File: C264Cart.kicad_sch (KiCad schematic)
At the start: 11 parts, among them J1 SJ, J2 SJ, J3 SJ, J4 SJ, J5 SJ, J6 SJ, U1 23128, U2 23128, U3 264-Exp-Port

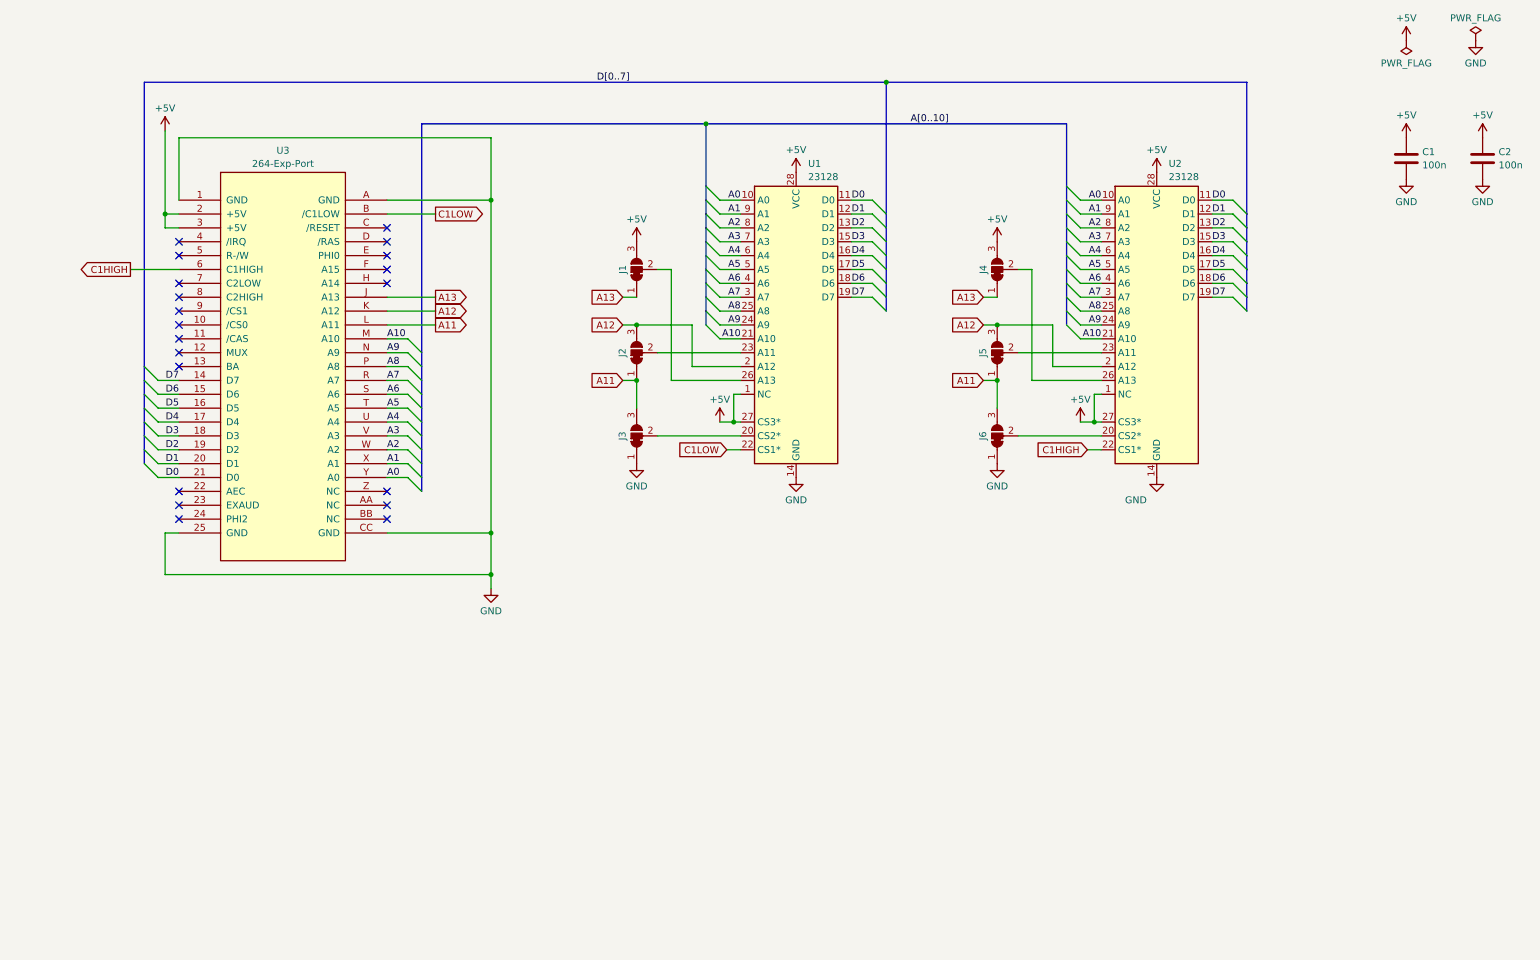
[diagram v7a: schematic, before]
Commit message: Working to use a single 'modern' 27C512-27C040 EEPROM.
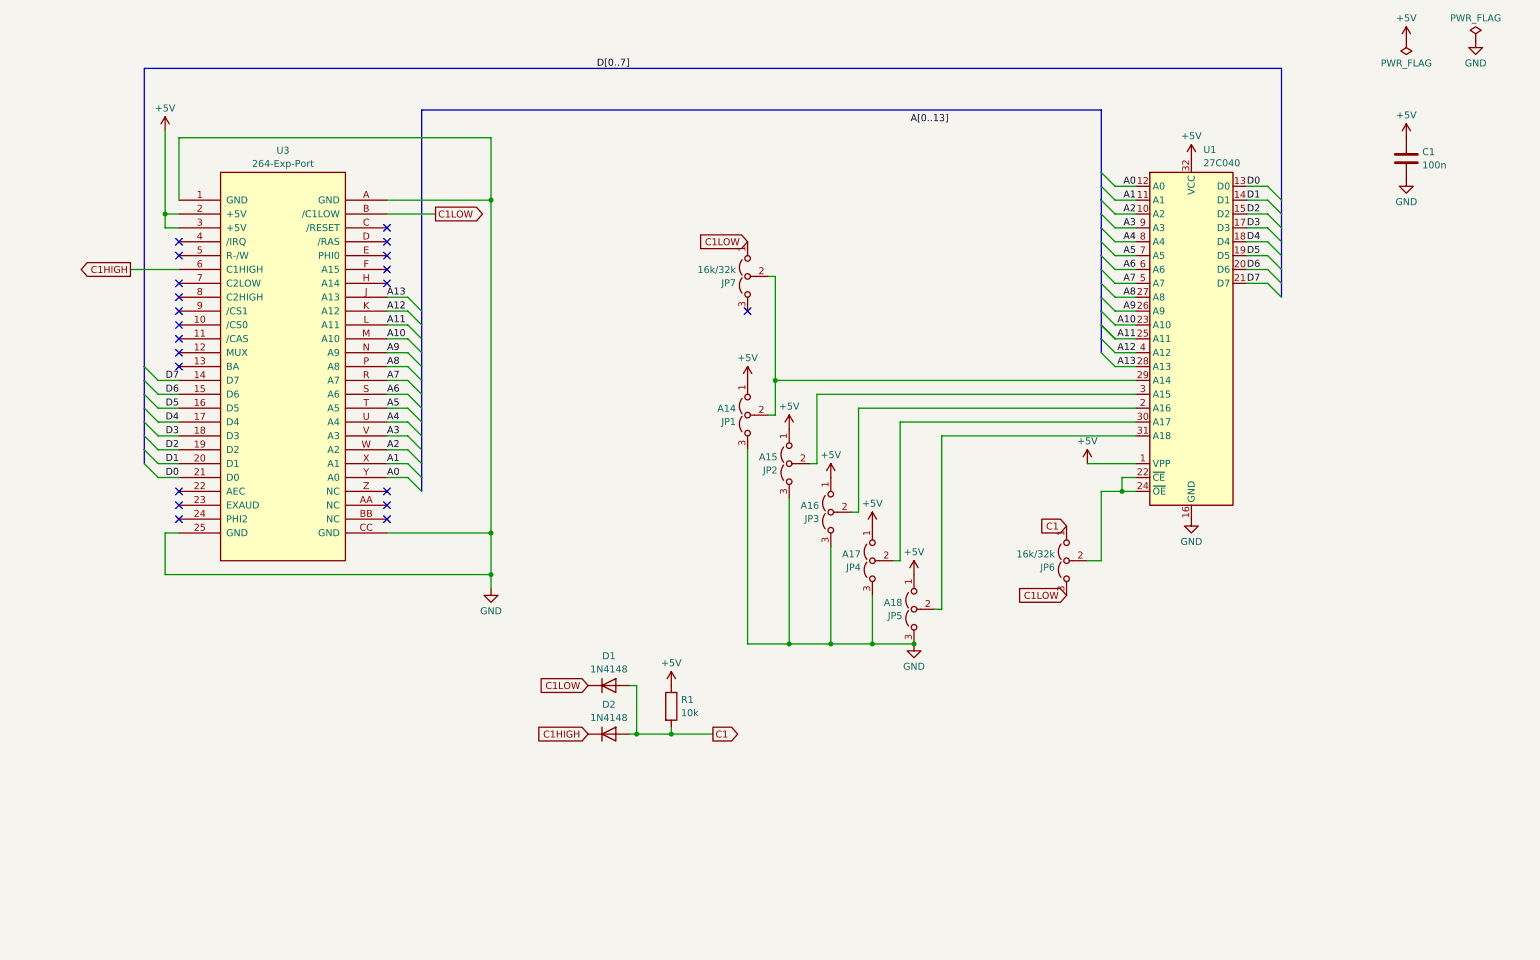
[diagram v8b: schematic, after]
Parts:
- removed C2: 100n, Capacitor_THT:C_Disc_D6.0mm_W2.5mm_P5.00mm, symbol Device:C
- removed J1, J4: SJ, C264Cart:SolderJumper-3_Bridged12-wide, symbol Jumper:SolderJumper_3_Bridged12
- removed J2, J5: SJ, C264Cart:SolderJumper-3_Bridged12, symbol Jumper:SolderJumper_3_Bridged12
- removed J3, J6: SJ, C264Cart:SolderJumper-3_Bridged12-narrow, symbol Jumper:SolderJumper_3_Bridged12
- removed U1, U2: 23128, Package_DIP:DIP-28_W15.24mm, symbol C264Cart:23128
- added D1, D2: 1N4148, Diode_THT:D_DO-35_SOD27_P7.62mm_Horizontal, symbol Device:D
- added JP1: A14, C264Cart:Jumper3_Solder, symbol Jumper:Jumper_3_Open
- added JP2: A15, C264Cart:Jumper3_Solder, symbol Jumper:Jumper_3_Open
- added JP3: A16, C264Cart:Jumper3_Solder, symbol Jumper:Jumper_3_Open
- added JP4: A17, C264Cart:Jumper3_Solder, symbol Jumper:Jumper_3_Open
- added JP5: A18, C264Cart:Jumper3_Solder, symbol Jumper:Jumper_3_Open
- added JP6, JP7: 16k/32k, C264Cart:Jumper3_Solder, symbol Jumper:Jumper_3_Open
- added R1: 10k, Resistor_THT:R_Axial_DIN0207_L6.3mm_D2.5mm_P7.62mm_Horizontal, symbol Device:R
- added U1: 27C040, C264Cart:DIP-28-32_W15.24mm, symbol Memory_EPROM:27C040
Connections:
- net +5V: now also JP1.1 (A), JP2.1 (A), JP3.1 (A), JP4.1 (A), JP5.1 (A), R1.1, U1.1 (VPP), U1.32 (VCC)
- net A0: now also U1.12 (A0)
- net A1: now also U1.11 (A1)
- net A10: now also U1.23 (A10)
- net A11: now also U1.25 (A11)
- net A12: now also U1.4 (A12)
- net A13: now also U1.28 (A13)
- net A2: now also U1.10 (A2)
- net A3: now also U1.9 (A3)
- net A4: now also U1.8 (A4)
- net A5: now also U1.7 (A5)
- net A6: now also U1.6 (A6)
- net A7: now also U1.5 (A7)
- net A8: now also U1.27 (A8)
- net A9: now also U1.26 (A9)
- net C1HIGH: now also D2.1 (K)
- net C1LOW: now also D1.1 (K), JP6.3 (B), JP7.1 (A)
- net D0: now also U1.13 (D0)
- net D1: now also U1.14 (D1)
- net D2: now also U1.15 (D2)
- net D3: now also U1.17 (D3)
- net D4: now also U1.18 (D4)
- net D5: now also U1.19 (D5)
- net D6: now also U1.20 (D6)
- net D7: now also U1.21 (D7)
- net GND: now also JP1.3 (B), JP2.3 (B), JP3.3 (B), JP4.3 (B), JP5.3 (B), U1.16 (GND)
- new net: JP5.2 (C), U1.31 (A18)
- new net: JP4.2 (C), U1.30 (A17)
- new net: JP1.2 (C), JP7.2 (C), U1.29 (A14)
- new net: JP3.2 (C), U1.2 (A16)
- new net: JP2.2 (C), U1.3 (A15)
- new net: JP6.2 (C), U1.22 (~{CE}), U1.24 (~{OE})
- new net C1: D1.2 (A), D2.2 (A), JP6.1 (A), R1.2
- no-connect marks 20 -> 21
